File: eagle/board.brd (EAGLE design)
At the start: 6 parts, among them J1 M20X2SHROUDED

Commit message: Adding rest of IO labels to board
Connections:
- net N$11 renamed GPIO25
- net N$12 renamed GPIO8/CE0
- net N$13 renamed GPIO7/CE1
- net N$14 renamed GPIO1/ID_SC
- net N$16 renamed GPIO12
- net N$18 renamed GPIO16/CE2
- net N$19 renamed GPIO20/MOSI
- net N$20 renamed GPIO21/SCLK
- net N$4 renamed GPIO14/TXD0
- net N$5 renamed GPIO15/RXD0
- net N$6 renamed GPIO18
- net N$8 renamed GPIO23
- net N$9 renamed GPIO24
- removed net N$10: J1.20
- removed net N$15: J1.30
- removed net N$17: J1.34
- removed net N$7: J1.14
- net GND: now also J1.14, J1.20, J1.30, J1.34
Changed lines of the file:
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@@
 <contactref element="J1" pad="39"/>
 <contactref element="J1" pad="25"/>
-<wire x1="-19.05" y1="11.43" x2="-19.05" y2="-6.35" width="0" layer="19" extent="1-1"/>
-<wire x1="-19.05" y1="31.75" x2="-19.05" y2="11.43" width="0" layer="19" extent="1-1"/>
+<contactref element="J1" pad="14"/>
+<contactref element="J1" pad="20"/>
+<contactref element="J1" pad="30"/>
+<contactref element="J1" pad="34"/>
+<wire x1="-16.51" y1="1.27" x2="-19.05" y2="-6.35" width="0" layer="19" extent="1-1"/>
+<wire x1="-16.51" y1="6.35" x2="-16.51" y2="1.27" width="0" layer="19" extent="1-1"/>
+<wire x1="-19.05" y1="11.43" x2="-16.51" y2="6.35" width="0" layer="19" extent="1-1"/>
+<wire x1="-16.51" y1="19.05" x2="-19.05" y2="11.43" width="0" layer="19" extent="1-1"/>
+<wire x1="-16.51" y1="26.67" x2="-16.51" y2="19.05" width="0" layer="19" extent="1-1"/>
+<wire x1="-19.05" y1="31.75" x2="-16.51" y2="26.67" width="0" layer="19" extent="1-1"/>
 <wire x1="-16.51" y1="36.83" x2="-19.05" y2="31.75" width="0" layer="19" extent="1-1"/>
 </signal>
-<signal name="N$4">
+<signal name="GPIO14/TXD0">
 <contactref element="J1" pad="8"/>
 </signal>
-<signal name="N$5">
+<signal name="GPIO15/RXD0">
 <contactref element="J1" pad="10"/>
 </signal>
-<signal name="N$6">
+<signal name="GPIO18">
 <contactref element="J1" pad="12"/>
 </signal>
-<signal name="N$7">
-<contactref element="J1" pad="14"/>
-</signal>
-<signal name="N$8">
+<signal name="GPIO23">
 <contactref element="J1" pad="16"/>
 </signal>
-<signal name="N$9">
+<signal name="GPIO24">
 <contactref element="J1" pad="18"/>
 </signal>
-<signal name="N$10">
-<contactref element="J1" pad="20"/>
-</signal>
-<signal name="N$11">
+<signal name="GPIO25">
 <contactref element="J1" pad="22"/>
 </signal>
-<signal name="N$12">
+<signal name="GPIO8/CE0">
 <contactref element="J1" pad="24"/>
 </signal>
-<signal name="N$13">
+<signal name="GPIO7/CE1">
 <contactref element="J1" pad="26"/>
 </signal>
-<signal name="N$14">
+<signal name="GPIO1/ID_SC">
 <contactref element="J1" pad="28"/>
 </signal>
-<signal name="N$15">
-<contactref element="J1" pad="30"/>
-</signal>
-<signal name="N$16">
+<signal name="GPIO12">
 <contactref element="J1" pad="32"/>
 </signal>
-<signal name="N$17">
-<contactref element="J1" pad="34"/>
-</signal>
-<signal name="N$18">
+<signal name="GPIO16/CE2">
 <contactref element="J1" pad="36"/>
 </signal>
-<signal name="N$19">
+<signal name="GPIO20/MOSI">
 <contactref element="J1" pad="38"/>
 </signal>
-<signal name="N$20">
+<signal name="GPIO21/SCLK">
 <contactref element="J1" pad="40"/>
 </signal>

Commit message: Renaming gnd/pwr signals so they don't route together
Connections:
- removed net +3V3: J1.1, J1.17
- removed net +5V: J1.2, J1.4
- removed net GND: J1.14, J1.20, J1.25, J1.30, J1.34, J1.39, J1.6, J1.9
- new net +3V3_0: J1.1
- new net +3V3_1: J1.17
- new net +5V_0: J1.2
- new net +5V_1: J1.4
- new net GND0: J1.9
- new net GND1: J1.25
- new net GND2: J1.39
- new net GND3: J1.6
- new net GND4: J1.14
- new net GND5: J1.20
- new net GND6: J1.30
- new net GND7: J1.34
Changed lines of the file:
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@@
 </elements>
 <signals>
-<signal name="+5V">
-<contactref element="J1" pad="2"/>
+<signal name="+5V_1">
 <contactref element="J1" pad="4"/>
-<wire x1="-16.51" y1="39.37" x2="-16.51" y2="41.91" width="0" layer="19" extent="1-1"/>
 </signal>
-<signal name="GND">
-<contactref element="J1" pad="6"/>
-<contactref element="J1" pad="9"/>
-<contactref element="J1" pad="39"/>
-<contactref element="J1" pad="25"/>
-<contactref element="J1" pad="14"/>
-<contactref element="J1" pad="20"/>
-<contactref element="J1" pad="30"/>
+<signal name="GND7">
 <contactref element="J1" pad="34"/>
-<wire x1="-16.51" y1="1.27" x2="-19.05" y2="-6.35" width="0" layer="19" extent="1-1"/>
-<wire x1="-16.51" y1="6.35" x2="-16.51" y2="1.27" width="0" layer="19" extent="1-1"/>
-<wire x1="-19.05" y1="11.43" x2="-16.51" y2="6.35" width="0" layer="19" extent="1-1"/>
-<wire x1="-16.51" y1="19.05" x2="-19.05" y2="11.43" width="0" layer="19" extent="1-1"/>
-<wire x1="-16.51" y1="26.67" x2="-16.51" y2="19.05" width="0" layer="19" extent="1-1"/>
-<wire x1="-19.05" y1="31.75" x2="-16.51" y2="26.67" width="0" layer="19" extent="1-1"/>
-<wire x1="-16.51" y1="36.83" x2="-19.05" y2="31.75" width="0" layer="19" extent="1-1"/>
 </signal>
 <signal name="GPIO14/TXD0">
@@
 <contactref element="J1" pad="40"/>
 </signal>
-<signal name="+3V3">
-<contactref element="J1" pad="1"/>
+<signal name="+3V3_1">
 <contactref element="J1" pad="17"/>
-<wire x1="-19.05" y1="21.59" x2="-19.05" y2="41.91" width="0" layer="19" extent="1-1"/>
 </signal>
 <signal name="GPIO2/SDA1">
@@
 <contactref element="J1" pad="19"/>
 </signal>
+<signal name="+3V3_0">
+<contactref element="J1" pad="1"/>
+</signal>
+<signal name="GND0">
+<contactref element="J1" pad="9"/>
+</signal>
+<signal name="GND1">
+<contactref element="J1" pad="25"/>
+</signal>
+<signal name="GND2">
+<contactref element="J1" pad="39"/>
+</signal>
+<signal name="+5V_0">
+<contactref element="J1" pad="2"/>
+</signal>
+<signal name="GND3">
+<contactref element="J1" pad="6"/>
+</signal>
+<signal name="GND4">
+<contactref element="J1" pad="14"/>
+</signal>
+<signal name="GND5">
+<contactref element="J1" pad="20"/>
+</signal>
+<signal name="GND6">
+<contactref element="J1" pad="30"/>
+</signal>
 </signals>

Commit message: Adding headers for modules
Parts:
- added DOOR, GSM, RFID: (no value), SparkFun-Connectors:1X06_LOCK
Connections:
- new net N$1: DOOR.6
- new net N$10: RFID.3
- new net N$11: RFID.2
- new net N$12: RFID.1
- new net N$13: GSM.6
- new net N$14: GSM.5
- new net N$15: GSM.4
- new net N$16: GSM.3
- new net N$17: GSM.2
- new net N$18: GSM.1
- new net N$2: DOOR.5
- new net N$3: DOOR.4
- new net N$4: DOOR.3
- new net N$5: DOOR.2
- new net N$6: DOOR.1
- new net N$7: RFID.6
- new net N$8: RFID.5
- new net N$9: RFID.4
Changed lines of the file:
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@@
 <element name="D1" library="SparkFun-LED" package="LED5MM" value="" x="-36.83" y="-25.4"/>
 <element name="D2" library="SparkFun-LED" package="LED5MM" value="" x="-36.83" y="-33.02"/>
+<element name="DOOR" library="SparkFun-Connectors" package="1X06_LOCK" value="" x="-38.1" y="-40.64"/>
+<element name="RFID" library="SparkFun-Connectors" package="1X06_LOCK" value="" x="-38.1" y="-45.72"/>
+<element name="GSM" library="SparkFun-Connectors" package="1X06_LOCK" value="" x="-38.1" y="-50.8"/>
 </elements>
 <signals>
@@
 <contactref element="J1" pad="30"/>
 </signal>
+<signal name="N$1">
+<contactref element="DOOR" pad="6"/>
+</signal>
+<signal name="N$2">
+<contactref element="DOOR" pad="5"/>
+</signal>
+<signal name="N$3">
+<contactref element="DOOR" pad="4"/>
+</signal>
+<signal name="N$4">
+<contactref element="DOOR" pad="3"/>
+</signal>
+<signal name="N$5">
+<contactref element="DOOR" pad="2"/>
+</signal>
+<signal name="N$6">
+<contactref element="DOOR" pad="1"/>
+</signal>
+<signal name="N$7">
+<contactref element="RFID" pad="6"/>
+</signal>
+<signal name="N$8">
+<contactref element="RFID" pad="5"/>
+</signal>
+<signal name="N$9">
+<contactref element="RFID" pad="4"/>
+</signal>
+<signal name="N$10">
+<contactref element="RFID" pad="3"/>
+</signal>
+<signal name="N$11">
+<contactref element="RFID" pad="2"/>
+</signal>
+<signal name="N$12">
+<contactref element="RFID" pad="1"/>
+</signal>
+<signal name="N$13">
+<contactref element="GSM" pad="6"/>
+</signal>
+<signal name="N$14">
+<contactref element="GSM" pad="5"/>
+</signal>
+<signal name="N$15">
+<contactref element="GSM" pad="4"/>
+</signal>
+<signal name="N$16">
+<contactref element="GSM" pad="3"/>
+</signal>
+<signal name="N$17">
+<contactref element="GSM" pad="2"/>
+</signal>
+<signal name="N$18">
+<contactref element="GSM" pad="1"/>
+</signal>
 </signals>

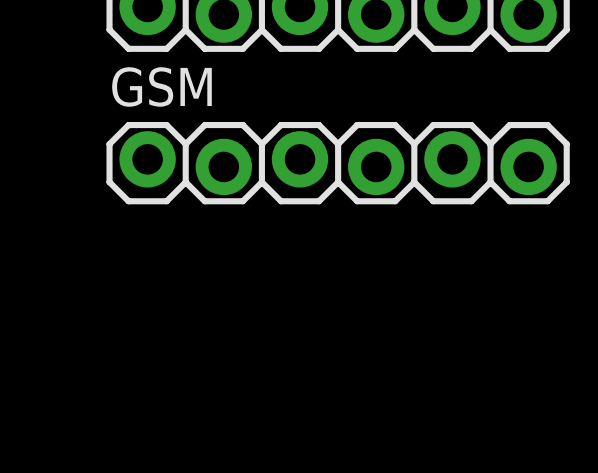
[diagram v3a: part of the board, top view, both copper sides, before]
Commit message: Add cap to switches for debounce
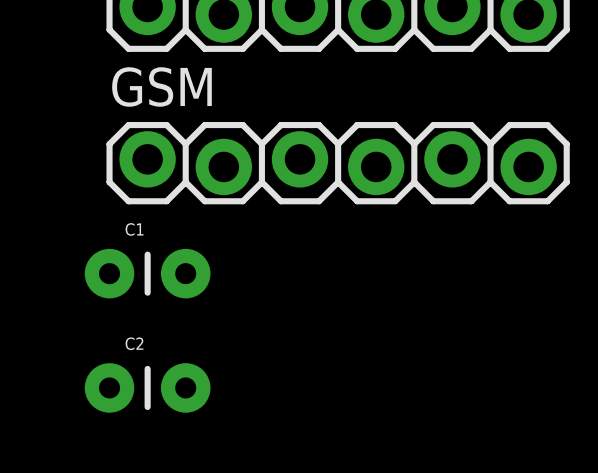
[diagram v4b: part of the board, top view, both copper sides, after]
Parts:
- added C1, C2: 10nF, SparkFun-Passives:CAP-PTH-SMALL
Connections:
- new net N$19: C1.2, S1.1
- new net N$20: C1.1, S1.3
- new net N$21: C2.1, S2.1
- new net N$22: C2.2, S2.3
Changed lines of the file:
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@@
 <element name="RFID" library="SparkFun-Connectors" package="1X06_LOCK" value="" x="-38.1" y="-45.72"/>
 <element name="GSM" library="SparkFun-Connectors" package="1X06_LOCK" value="" x="-38.1" y="-50.8"/>
+<element name="C1" library="SparkFun-Passives" package="CAP-PTH-SMALL" value="10nF" x="-39.37" y="-54.61"/>
+<element name="C2" library="SparkFun-Passives" package="CAP-PTH-SMALL" value="10nF" x="-39.37" y="-58.42"/>
 </elements>
 <signals>
@@
 <contactref element="GSM" pad="1"/>
 </signal>
+<signal name="N$19">
+<contactref element="S1" pad="1"/>
+<contactref element="C1" pad="2"/>
+<wire x1="-31.1912" y1="-6.6294" x2="-36.83" y2="-54.61" width="0" layer="19" extent="1-1"/>
+</signal>
+<signal name="N$20">
+<contactref element="S1" pad="3"/>
+<contactref element="C1" pad="1"/>
+<wire x1="-31.1912" y1="-11.1506" x2="-39.37" y2="-54.61" width="0" layer="19" extent="1-1"/>
+</signal>
+<signal name="N$21">
+<contactref element="S2" pad="1"/>
+<contactref element="C2" pad="1"/>
+<wire x1="-40.0812" y1="-6.6294" x2="-39.37" y2="-58.42" width="0" layer="19" extent="1-1"/>
+</signal>
+<signal name="N$22">
+<contactref element="S2" pad="3"/>
+<contactref element="C2" pad="2"/>
+<wire x1="-40.0812" y1="-11.1506" x2="-36.83" y2="-58.42" width="0" layer="19" extent="1-1"/>
+</signal>
 </signals>

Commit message: Rename nets on ribbon connector
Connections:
- net GPIO1/ID_SC renamed GPIO1
- net GPIO10/MOSI renamed GPIO10
- net GPIO11/SCLK renamed GPIO11
- net GPIO14/TXD0 renamed TXD0
- net GPIO15/RXD0 renamed RXD0
- net GPIO16/CE2 renamed GPIO16
- net GPIO19/MISO renamed GPIO19
- net GPIO2/SDA1 renamed GPIO2
- net GPIO20/MOSI renamed GPIO20
- net GPIO21/SCLK renamed GPIO21
- net GPIO3/SCL1 renamed GPIO3
- net GPIO7/CE1 renamed GPIO7
- net GPIO8/CE0 renamed GPIO8
- net GPIO9/MISO renamed GPIO09
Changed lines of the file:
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@@
 <contactref element="J1" pad="34"/>
 </signal>
-<signal name="GPIO14/TXD0">
+<signal name="TXD0">
 <contactref element="J1" pad="8"/>
 </signal>
-<signal name="GPIO15/RXD0">
+<signal name="RXD0">
 <contactref element="J1" pad="10"/>
 </signal>
@@
 <contactref element="J1" pad="22"/>
 </signal>
-<signal name="GPIO8/CE0">
+<signal name="GPIO8">
 <contactref element="J1" pad="24"/>
 </signal>
-<signal name="GPIO7/CE1">
+<signal name="GPIO7">
 <contactref element="J1" pad="26"/>
 </signal>
-<signal name="GPIO1/ID_SC">
+<signal name="GPIO1">
 <contactref element="J1" pad="28"/>
 </signal>
@@
 <contactref element="J1" pad="32"/>
 </signal>
-<signal name="GPIO16/CE2">
+<signal name="GPIO16">
 <contactref element="J1" pad="36"/>
 </signal>
-<signal name="GPIO20/MOSI">
+<signal name="GPIO20">
 <contactref element="J1" pad="38"/>
 </signal>
-<signal name="GPIO21/SCLK">
+<signal name="GPIO21">
 <contactref element="J1" pad="40"/>
 </signal>
@@
 <contactref element="J1" pad="17"/>
 </signal>
-<signal name="GPIO2/SDA1">
+<signal name="GPIO2">
 <contactref element="J1" pad="3"/>
 </signal>
-<signal name="GPIO3/SCL1">
+<signal name="GPIO3">
 <contactref element="J1" pad="5"/>
 </signal>
@@
 <contactref element="J1" pad="15"/>
 </signal>
-<signal name="GPIO9/MISO">
+<signal name="GPIO09">
 <contactref element="J1" pad="21"/>
 </signal>
-<signal name="GPIO11/SCLK">
+<signal name="GPIO11">
 <contactref element="J1" pad="23"/>
 </signal>
@@
 <contactref element="J1" pad="33"/>
 </signal>
-<signal name="GPIO19/MISO">
+<signal name="GPIO19">
 <contactref element="J1" pad="35"/>
 </signal>
@@
 <contactref element="J1" pad="37"/>
 </signal>
-<signal name="GPIO10/MOSI">
+<signal name="GPIO10">
 <contactref element="J1" pad="19"/>
 </signal>

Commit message: Connect door header
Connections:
- net N$3 renamed GND
- net N$6 renamed VCC
- removed net N$2: DOOR.5
- removed net N$4: DOOR.3
- removed net N$5: DOOR.2
- net GPIO12: now also DOOR.5
- net GPIO20: now also DOOR.2
- net GPIO21: now also DOOR.3
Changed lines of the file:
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@@
 <signal name="GPIO12">
 <contactref element="J1" pad="32"/>
+<contactref element="DOOR" pad="5"/>
+<wire x1="-16.51" y1="3.81" x2="-27.94" y2="-40.64" width="0" layer="19" extent="1-1"/>
 </signal>
 <signal name="GPIO16">
@@
 <signal name="GPIO20">
 <contactref element="J1" pad="38"/>
+<contactref element="DOOR" pad="2"/>
+<wire x1="-16.51" y1="-3.81" x2="-35.56" y2="-40.894" width="0" layer="19" extent="1-1"/>
 </signal>
 <signal name="GPIO21">
 <contactref element="J1" pad="40"/>
+<contactref element="DOOR" pad="3"/>
+<wire x1="-16.51" y1="-6.35" x2="-33.02" y2="-40.64" width="0" layer="19" extent="1-1"/>
 </signal>
 <signal name="+3V3_1">
@@
 <contactref element="DOOR" pad="6"/>
 </signal>
-<signal name="N$2">
-<contactref element="DOOR" pad="5"/>
-</signal>
-<signal name="N$3">
+<signal name="GND">
 <contactref element="DOOR" pad="4"/>
 </signal>
-<signal name="N$4">
-<contactref element="DOOR" pad="3"/>
-</signal>
-<signal name="N$5">
-<contactref element="DOOR" pad="2"/>
-</signal>
-<signal name="N$6">
+<signal name="VCC">
 <contactref element="DOOR" pad="1"/>
 </signal>

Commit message: Connect rfid header
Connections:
- removed net N$10: RFID.3
- removed net N$11: RFID.2
- removed net N$12: RFID.1
- removed net N$7: RFID.6
- removed net N$8: RFID.5
- removed net N$9: RFID.4
- net GND: now also RFID.2
- net GPIO18: now also RFID.3
- net GPIO23: now also RFID.4
- net GPIO24: now also RFID.5
- net GPIO25: now also RFID.6
- net VCC: now also RFID.1
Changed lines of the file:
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@@
 <signal name="GPIO18">
 <contactref element="J1" pad="12"/>
+<contactref element="RFID" pad="3"/>
+<wire x1="-16.51" y1="29.21" x2="-33.02" y2="-45.72" width="0" layer="19" extent="1-1"/>
 </signal>
 <signal name="GPIO23">
 <contactref element="J1" pad="16"/>
+<contactref element="RFID" pad="4"/>
+<wire x1="-16.51" y1="24.13" x2="-30.48" y2="-45.974" width="0" layer="19" extent="1-1"/>
 </signal>
 <signal name="GPIO24">
 <contactref element="J1" pad="18"/>
+<contactref element="RFID" pad="5"/>
+<wire x1="-16.51" y1="21.59" x2="-27.94" y2="-45.72" width="0" layer="19" extent="1-1"/>
 </signal>
 <signal name="GPIO25">
 <contactref element="J1" pad="22"/>
+<contactref element="RFID" pad="6"/>
+<wire x1="-16.51" y1="16.51" x2="-25.4" y2="-45.974" width="0" layer="19" extent="1-1"/>
 </signal>
 <signal name="GPIO8">
@@
 <signal name="GND">
 <contactref element="DOOR" pad="4"/>
+<contactref element="RFID" pad="2"/>
+<wire x1="-30.48" y1="-40.894" x2="-35.56" y2="-45.974" width="0" layer="19" extent="1-1"/>
 </signal>
 <signal name="VCC">
 <contactref element="DOOR" pad="1"/>
-</signal>
-<signal name="N$7">
-<contactref element="RFID" pad="6"/>
-</signal>
-<signal name="N$8">
-<contactref element="RFID" pad="5"/>
-</signal>
-<signal name="N$9">
-<contactref element="RFID" pad="4"/>
-</signal>
-<signal name="N$10">
-<contactref element="RFID" pad="3"/>
-</signal>
-<signal name="N$11">
-<contactref element="RFID" pad="2"/>
-</signal>
-<signal name="N$12">
 <contactref element="RFID" pad="1"/>
+<wire x1="-38.1" y1="-40.64" x2="-38.1" y2="-45.72" width="0" layer="19" extent="1-1"/>
 </signal>
 <signal name="N$13">

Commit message: Connect gsm header
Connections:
- removed net N$15: GSM.4
- removed net N$16: GSM.3
- removed net N$17: GSM.2
- removed net N$18: GSM.1
- net GND: now also GSM.1
- net RXD0: now also GSM.4
- net TXD0: now also GSM.3
- net VCC: now also GSM.2
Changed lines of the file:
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@@
 <signal name="TXD0">
 <contactref element="J1" pad="8"/>
+<contactref element="GSM" pad="3"/>
+<wire x1="-16.51" y1="34.29" x2="-33.02" y2="-50.8" width="0" layer="19" extent="1-1"/>
 </signal>
 <signal name="RXD0">
 <contactref element="J1" pad="10"/>
+<contactref element="GSM" pad="4"/>
+<wire x1="-16.51" y1="31.75" x2="-30.48" y2="-51.054" width="0" layer="19" extent="1-1"/>
 </signal>
 <signal name="GPIO18">
@@
 <contactref element="DOOR" pad="4"/>
 <contactref element="RFID" pad="2"/>
+<contactref element="GSM" pad="1"/>
+<wire x1="-35.56" y1="-45.974" x2="-38.1" y2="-50.8" width="0" layer="19" extent="1-1"/>
 <wire x1="-30.48" y1="-40.894" x2="-35.56" y2="-45.974" width="0" layer="19" extent="1-1"/>
 </signal>
@@
 <contactref element="DOOR" pad="1"/>
 <contactref element="RFID" pad="1"/>
+<contactref element="GSM" pad="2"/>
+<wire x1="-38.1" y1="-45.72" x2="-35.56" y2="-51.054" width="0" layer="19" extent="1-1"/>
 <wire x1="-38.1" y1="-40.64" x2="-38.1" y2="-45.72" width="0" layer="19" extent="1-1"/>
 </signal>
@@
 <contactref element="GSM" pad="5"/>
 </signal>
-<signal name="N$15">
-<contactref element="GSM" pad="4"/>
-</signal>
-<signal name="N$16">
-<contactref element="GSM" pad="3"/>
-</signal>
-<signal name="N$17">
-<contactref element="GSM" pad="2"/>
-</signal>
-<signal name="N$18">
-<contactref element="GSM" pad="1"/>
-</signal>
 <signal name="N$19">
